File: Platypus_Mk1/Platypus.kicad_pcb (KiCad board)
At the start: 4 copper layers, 75 x 57 mm, 63 parts, among them CN1 SERVO_PWM, CN10 FEMALE_LEFT, CN11 FEMALE_RIGHT, CN12 LASER_CONN, CN2 CFG1, CN3 CFG1, CN4 CFG1, CN5 FEMALE_LEFT, CN6 FEMALE_RIGHT, CN7 CFG1, CN8 CFG1, CN9 CFG1, J1 PJ-202AH, J10 ICSP, J11 MotorTerm, J12 MotorHeader, J13 MotorTerm, J14 MotorHeader, J15 12V_TERM, J2 TermLaser, J3 TermStop, J4 LASER_PWR, J5 LASER_PULSE, J6 TermControl, J7 TermLimit, J8 TermAux, J9 UJ2-BH-1-TH, K1 SW_RESET, U1 CJ7805, U2 INTERFACE-CH340T_SSOP20_, U3 MCU-ATMEGA328P-AU_TQFP32_, Y1 12MHz, Y2 16MHZ

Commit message: Addinge license note to board back
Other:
- board text added: "Licensed Under CERN OHL v1.2"
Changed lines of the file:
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@@
   (general
     (thickness 1.6)
-    (drawings 120)
+    (drawings 121)
     (tracks 596)
     (zones 0)
@@
     (34 B.Paste user)
     (35 F.Paste user)
-    (36 B.SilkS user hide)
+    (36 B.SilkS user)
     (37 F.SilkS user)
     (38 B.Mask user)
@@
     (visible_elements 7FFFFF7F)
     (pcbplotparams
-      (layerselection 0x01020_7ffffff8)
+      (layerselection 0x01010_7ffffff8)
       (usegerberextensions false)
       (usegerberattributes false)
@@
       (padsonsilk false)
       (subtractmaskfromsilk false)
-      (outputformat 4)
+      (outputformat 1)
       (mirror false)
       (drillshape 0)
@@
     )
   )
+  (gr_text "Licensed Under CERN OHL v1.2" (at 216.916 48.387 270) (layer B.SilkS)
+    (effects (font (size 1.1 1.1) (thickness 0.275)) (justify mirror))
+  )
   (gr_text ManiacalLabs.com/Platypus (at 182.372 75.692) (layer B.SilkS)

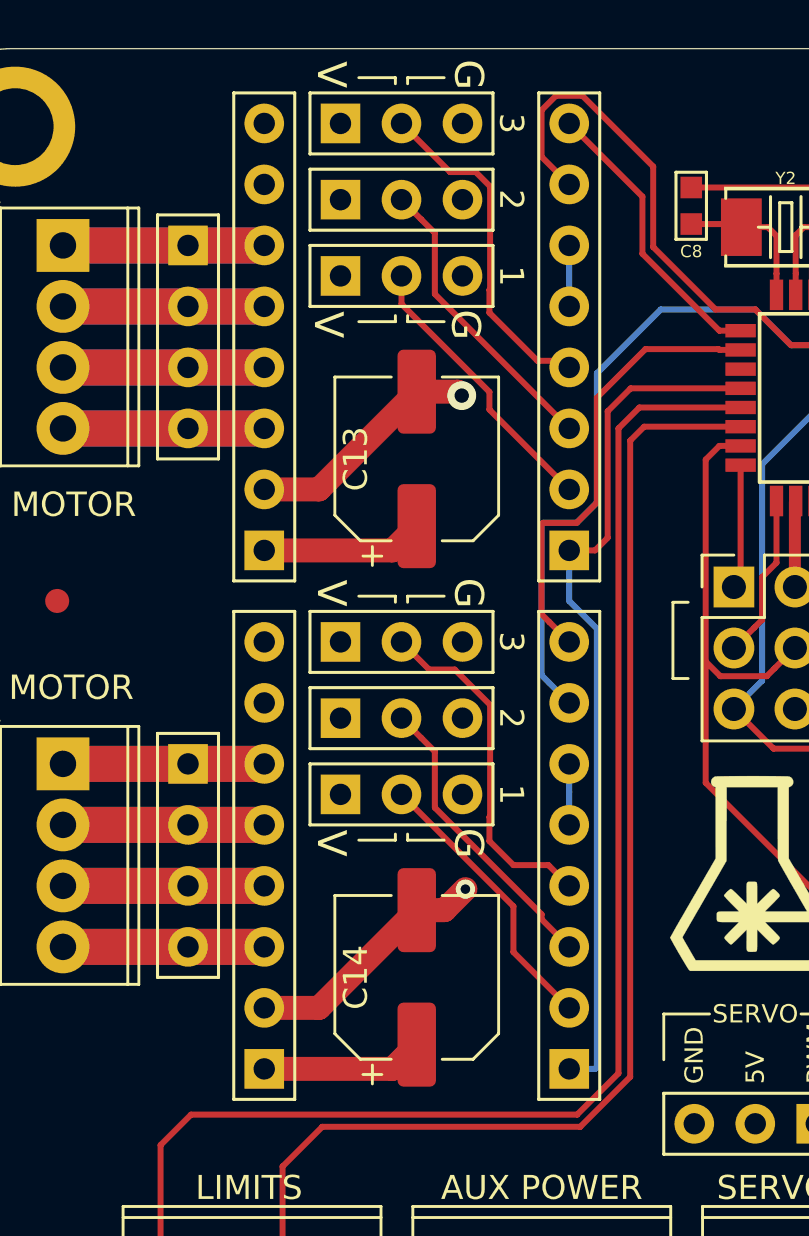
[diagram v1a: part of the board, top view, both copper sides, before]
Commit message: Adding stepper driver labels
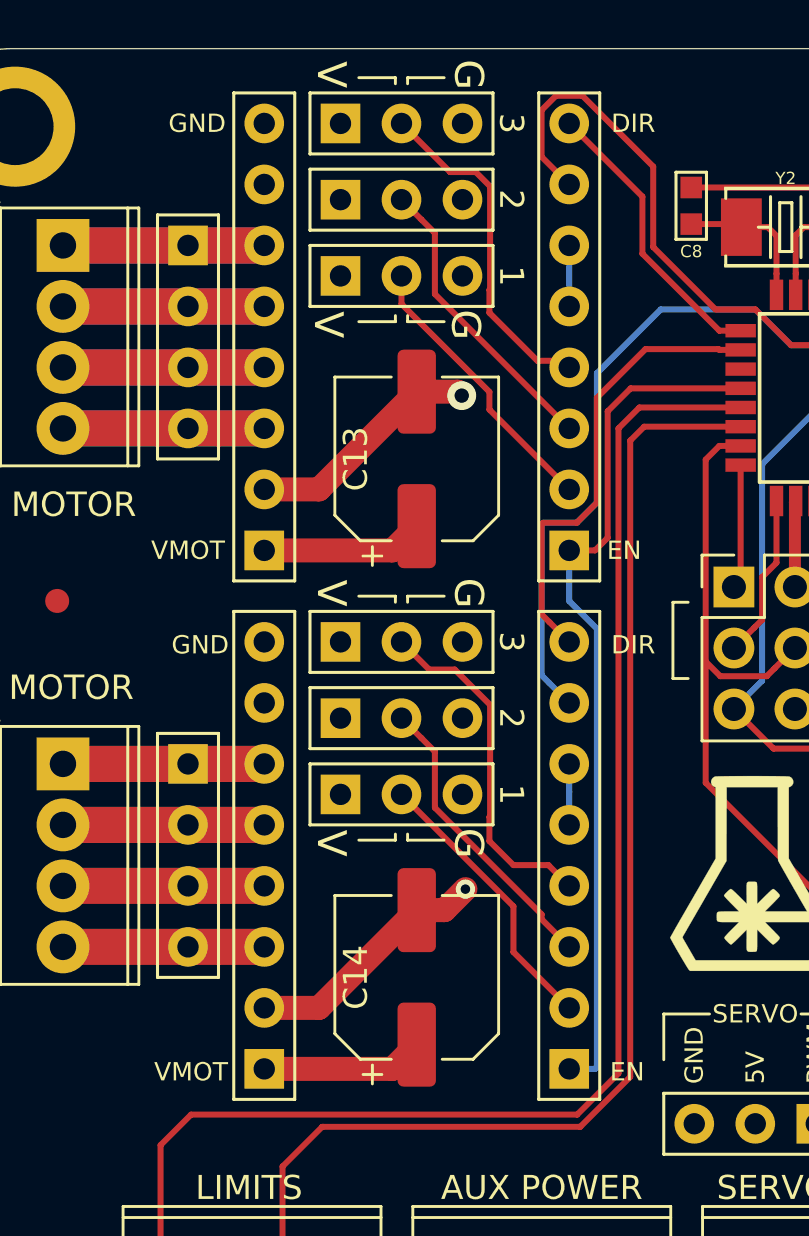
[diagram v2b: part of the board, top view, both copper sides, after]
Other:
- board text added: "DIR"
- board text added: "EN"
- board text added: "VMOT"
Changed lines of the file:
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@@
-(kicad_pcb (version 20171130) (host pcbnew 5.1.2-1.fc30)
+(kicad_pcb (version 20171130) (host pcbnew "(5.1.2)-2")
   (general
     (thickness 1.6)
-    (drawings 121)
+    (drawings 129)
     (tracks 596)
     (zones 0)
@@
     (visible_elements 7FFFFF7F)
     (pcbplotparams
-      (layerselection 0x01010_7ffffff8)
+      (layerselection 0x00020_7ffffff8)
       (usegerberextensions false)
       (usegerberattributes false)
@@
     )
   )
+  (gr_text EN (at 173.736 70.612) (layer F.SilkS)
+    (effects (font (size 0.762 0.762) (thickness 0.15)))
+  )
+  (gr_text GND (at 155.956 52.832) (layer F.SilkS)
+    (effects (font (size 0.762 0.762) (thickness 0.15)))
+  )
+  (gr_text DIR (at 173.99 52.832) (layer F.SilkS)
+    (effects (font (size 0.762 0.762) (thickness 0.15)))
+  )
+  (gr_text VMOT (at 155.575 70.612) (layer F.SilkS)
+    (effects (font (size 0.762 0.762) (thickness 0.15)))
+  )
+  (gr_text DIR (at 173.99 31.115) (layer F.SilkS)
+    (effects (font (size 0.762 0.762) (thickness 0.15)))
+  )
+  (gr_text GND (at 155.829 31.115) (layer F.SilkS)
+    (effects (font (size 0.762 0.762) (thickness 0.15)))
+  )
+  (gr_text EN (at 173.609 48.895) (layer F.SilkS)
+    (effects (font (size 0.762 0.762) (thickness 0.15)))
+  )
+  (gr_text VMOT (at 155.448 48.895) (layer F.SilkS)
+    (effects (font (size 0.762 0.762) (thickness 0.15)))
+  )
   (gr_text "Licensed Under CERN OHL v1.2" (at 216.916 48.387 270) (layer B.SilkS)

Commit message: Adding dimensions doc
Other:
- board text added: "3.2mm"
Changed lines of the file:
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@@
-(kicad_pcb (version 20171130) (host pcbnew "(5.1.2)-2")
+(kicad_pcb (version 20171130) (host pcbnew "(5.1.4)-1")
   (general
     (thickness 1.6)
-    (drawings 129)
+    (drawings 138)
     (tracks 596)
     (zones 0)
@@
     )
   )
+  (gr_circle (center 216.75 31.25) (end 218 32) (layer Eco1.User) (width 0.15))
+  (gr_circle (center 216.75 81.75) (end 217.5 83) (layer Eco1.User) (width 0.15))
+  (gr_circle (center 148.25 81.75) (end 149 83) (layer Eco1.User) (width 0.15))
+  (gr_circle (center 148.25 31.25) (end 149 32.5) (layer Eco1.User) (width 0.15))
+  (gr_text 3.2mm (at 141 26) (layer Eco1.User)
+    (effects (font (size 1 1) (thickness 0.15)))
+  )
+  (gr_line (start 144.5 28.5) (end 143 27) (layer Eco1.User) (width 0.15))
+  (gr_line (start 144 28.5) (end 144.5 28.5) (layer Eco1.User) (width 0.15))
+  (gr_line (start 144.5 28) (end 144 28.5) (layer Eco1.User) (width 0.15))
+  (gr_line (start 144.5 28.5) (end 144.5 28) (layer Eco1.User) (width 0.15))
   (gr_text EN (at 173.736 70.612) (layer F.SilkS)
     (effects (font (size 0.762 0.762) (thickness 0.15)))
